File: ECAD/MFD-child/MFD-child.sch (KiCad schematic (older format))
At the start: 44 parts, among them J1 ICSP, J2 Conn_01x05, J3 Conn_01x05, SW1 RESET, SW11 OSB1, SW12 OSB2, SW13 OSB3, SW14 OSB4, SW15 OSB5, SW16 SYM-UP, SW17 SYM-DN, SW2 SW_Coded_SH-7010, SW21 OSB6, SW22 OSB7, SW23 OSB8, SW24 OSB9, SW25 OSB10, SW26 CON-UP, SW27 CON-DN, SW31 OSB11, SW32 OSB12, SW33 OSB13, SW34 OSB14, SW35 OSB15, SW36 BRT-UP, SW37 BRT-DN, SW41 OSB16, SW42 OSB17, SW43 OSB18, SW44 OSB19, SW45 OSB20, SW46 GAIN-UP, SW47 GAIN-DN

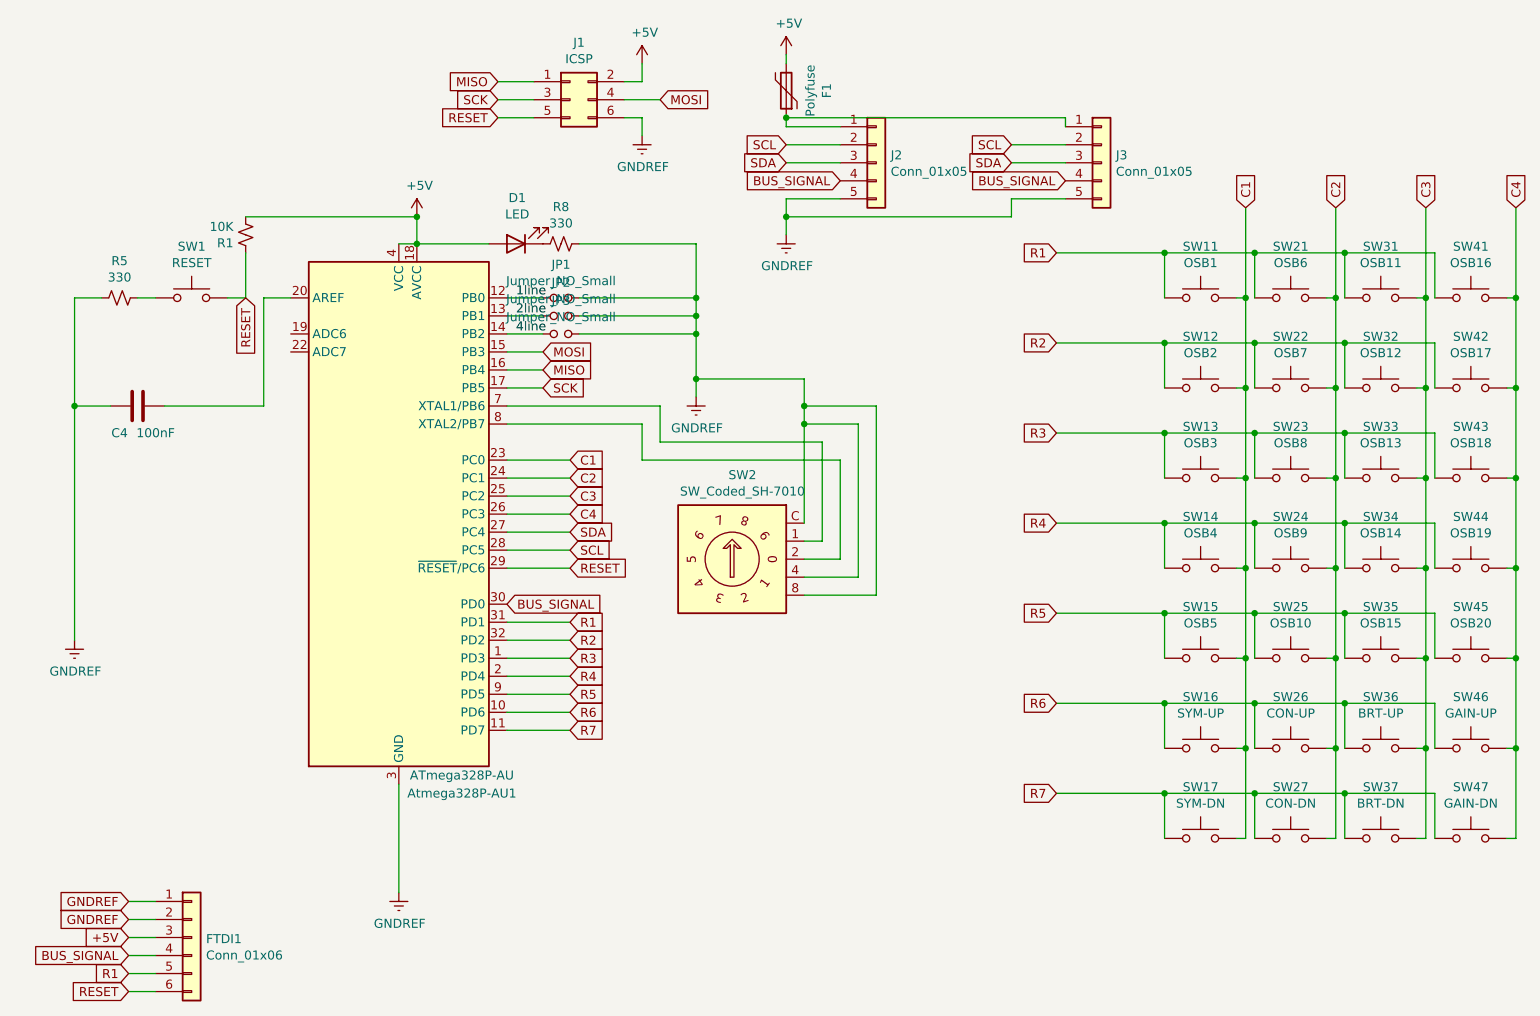
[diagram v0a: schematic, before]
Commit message: Swap bus connector to 4-pin JST-GH
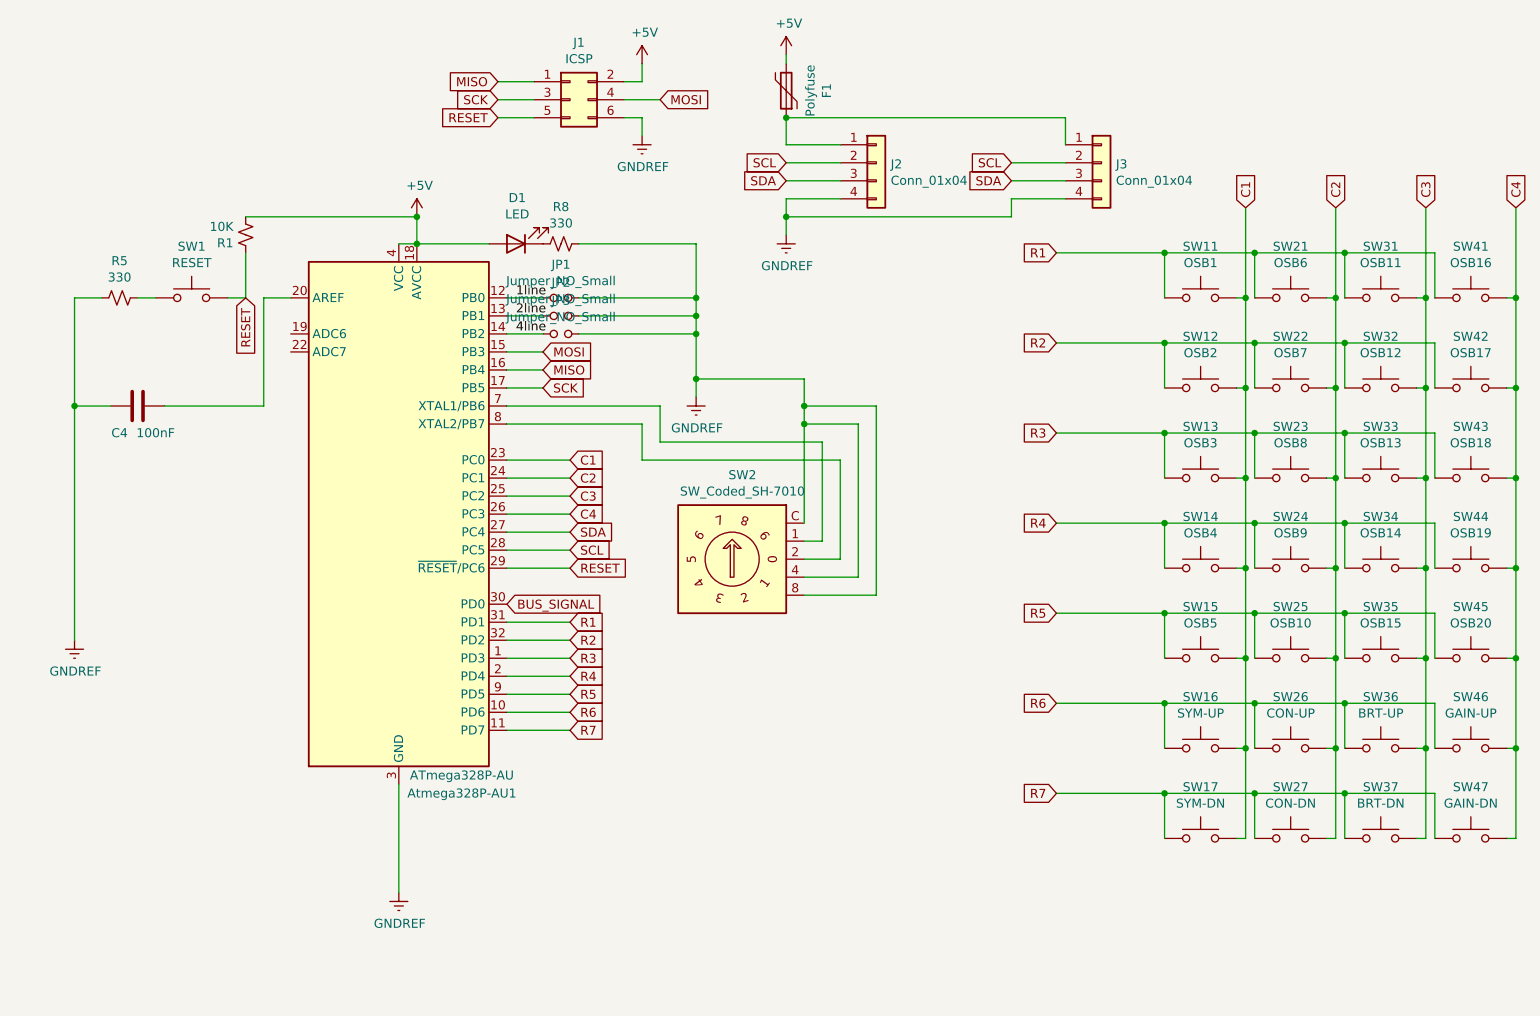
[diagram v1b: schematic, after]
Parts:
- removed FTDI1: Conn_01x06, Connector_PinHeader_2.54mm:PinHeader_1x06_P2.54mm_Vertical, symbol Connector_Generic:Conn_01x06
- removed J2, J3: Conn_01x05, Connector_JST:JST_GH_SM05B-GHS-TB_1x05-1MP_P1.25mm_Horizontal, symbol Connector_Generic:Conn_01x05
- added J2, J3: Conn_01x04, Connector_JST:JST_GH_SM04B-GHS-TB_1x04-1MP_P1.25mm_Horizontal, symbol Connector_Generic:Conn_01x04
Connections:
- net GNDREF: now also J2.4 (Pin_4), J3.4 (Pin_4)
- net SCL: now also J2.2 (Pin_2), J3.2 (Pin_2)
- net SDA: now also J2.3 (Pin_3), J3.3 (Pin_3)
- net at F1.1: now also J2.1 (Pin_1), J3.1 (Pin_1)
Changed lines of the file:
@@
 Text GLabel 5250 3700 2    50   Input ~ 0
 BUS_SIGNAL
-Wire Wire Line
-	3150 5850 3300 5850
-Wire Wire Line
-	3150 5750 3300 5750
-Wire Wire Line
-	3150 5650 3300 5650
-Wire Wire Line
-	3150 5550 3300 5550
-Wire Wire Line
-	3150 5450 3300 5450
-Text GLabel 3150 5450 0    50   Input ~ 0
-GNDREF
-Wire Wire Line
-	3150 5350 3300 5350
-Text GLabel 3150 5350 0    50   Input ~ 0
-GNDREF
-$Comp
-L Connector_Generic:Conn_01x06 FTDI1
-U 1 1 6116595E
-P 3500 5550
-F 0 "FTDI1" H 3580 5542 50  0000 L CNN
-F 1 "Conn_01x06" H 3580 5451 50  0000 L CNN
-F 2 "Connector_PinHeader_2.54mm:PinHeader_1x06_P2.54mm_Vertical" H 3500 5550 50  0001 C CNN
-F 3 "~" H 3500 5550 50  0001 C CNN
-	1    3500 5550
-	1    0    0    -1
-$EndComp
-Text GLabel 3150 5550 0    50   Input ~ 0
-+5V
-Text GLabel 3150 5850 0    50   Input ~ 0
-RESET
-Text GLabel 3150 5650 0    50   Input ~ 0
-BUS_SIGNAL
-Text GLabel 3150 5750 0    50   Input ~ 0
-R1
 $Comp
 L power:+5V #PWR0102
@@
 F 3 "" H 6800 650 50  0001 C CNN
 	1    6800 650
-	1    0    0    -1
-$EndComp
-Text GLabel 7100 1350 0    50   Input ~ 0
-BUS_SIGNAL
-$Comp
-L Connector_Generic:Conn_01x05 J2
-U 1 1 61241877
-P 7300 1250
-F 0 "J2" H 7380 1292 50  0000 L CNN
-F 1 "Conn_01x05" H 7380 1201 50  0000 L CNN
-F 2 "Connector_JST:JST_GH_SM05B-GHS-TB_1x05-1MP_P1.25mm_Horizontal" H 7300 1250 50  0001 C CNN
-F 3 "~" H 7300 1250 50  0001 C CNN
-	1    7300 1250
 	1    0    0    -1
 $EndComp
@@
 $EndComp
 Wire Wire Line
-	7100 1250 6800 1250
+	7100 1350 6800 1350
 Wire Wire Line
-	6800 1150 7100 1150
+	6800 1250 7100 1250
+Text GLabel 6800 1350 0    50   Input ~ 0
+SDA
 Text GLabel 6800 1250 0    50   Input ~ 0
-SDA
-Text GLabel 6800 1150 0    50   Input ~ 0
 SCL
 Wire Wire Line
@@
 Wire Wire Line
 	8050 1450 8050 1550
-Text GLabel 8050 1150 0    50   Input ~ 0
-SCL
-Text GLabel 8050 1250 0    50   Input ~ 0
-SDA
-Wire Wire Line
-	8050 1150 8350 1150
-Wire Wire Line
-	8350 1250 8050 1250
-$Comp
-L Connector_Generic:Conn_01x05 J3
-U 1 1 61241894
-P 8550 1250
-F 0 "J3" H 8630 1292 50  0000 L CNN
-F 1 "Conn_01x05" H 8630 1201 50  0000 L CNN
-F 2 "Connector_JST:JST_GH_SM05B-GHS-TB_1x05-1MP_P1.25mm_Horizontal" H 8550 1250 50  0001 C CNN
-F 3 "~" H 8550 1250 50  0001 C CNN
-	1    8550 1250
-	1    0    0    -1
-$EndComp
-Text GLabel 8350 1350 0    50   Input ~ 0
-BUS_SIGNAL
 Wire Wire Line
 	6800 1450 6800 1550
@@
 	6800 700  6800 650
 Wire Wire Line
-	6800 1000 6800 1050
-Wire Wire Line
-	6800 1050 7100 1050
-Wire Wire Line
-	8350 1050 8350 1000
+	6800 1150 7100 1150
 Wire Wire Line
 	8350 1000 6800 1000
+$Comp
+L Connector_Generic:Conn_01x04 J2
+U 1 1 611D0BB4
+P 7300 1250
+F 0 "J2" H 7380 1242 50  0000 L CNN
+F 1 "Conn_01x04" H 7380 1151 50  0000 L CNN
+F 2 "Connector_JST:JST_GH_SM04B-GHS-TB_1x04-1MP_P1.25mm_Horizontal" H 7300 1250 50  0001 C CNN
+F 3 "~" H 7300 1250 50  0001 C CNN
+	1    7300 1250
+	1    0    0    -1
+$EndComp
+Wire Wire Line
+	6800 1000 6800 1150
 Connection ~ 6800 1000
+$Comp
+L Connector_Generic:Conn_01x04 J3
+U 1 1 611E9B82
+P 8550 1250
+F 0 "J3" H 8630 1242 50  0000 L CNN
+F 1 "Conn_01x04" H 8630 1151 50  0000 L CNN
+F 2 "Connector_JST:JST_GH_SM04B-GHS-TB_1x04-1MP_P1.25mm_Horizontal" H 8550 1250 50  0001 C CNN
+F 3 "~" H 8550 1250 50  0001 C CNN
+	1    8550 1250
+	1    0    0    -1
+$EndComp
+Wire Wire Line
+	8350 1350 8050 1350
+Wire Wire Line
+	8050 1250 8350 1250
+Text GLabel 8050 1350 0    50   Input ~ 0
+SDA
+Text GLabel 8050 1250 0    50   Input ~ 0
+SCL
+Wire Wire Line
+	8350 1000 8350 1150
 $EndSCHEMATC
